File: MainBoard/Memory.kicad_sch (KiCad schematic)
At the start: 9 parts, among them U2 74AHCT04, U68 ATF22V10C, U69 CD74HC173PWR

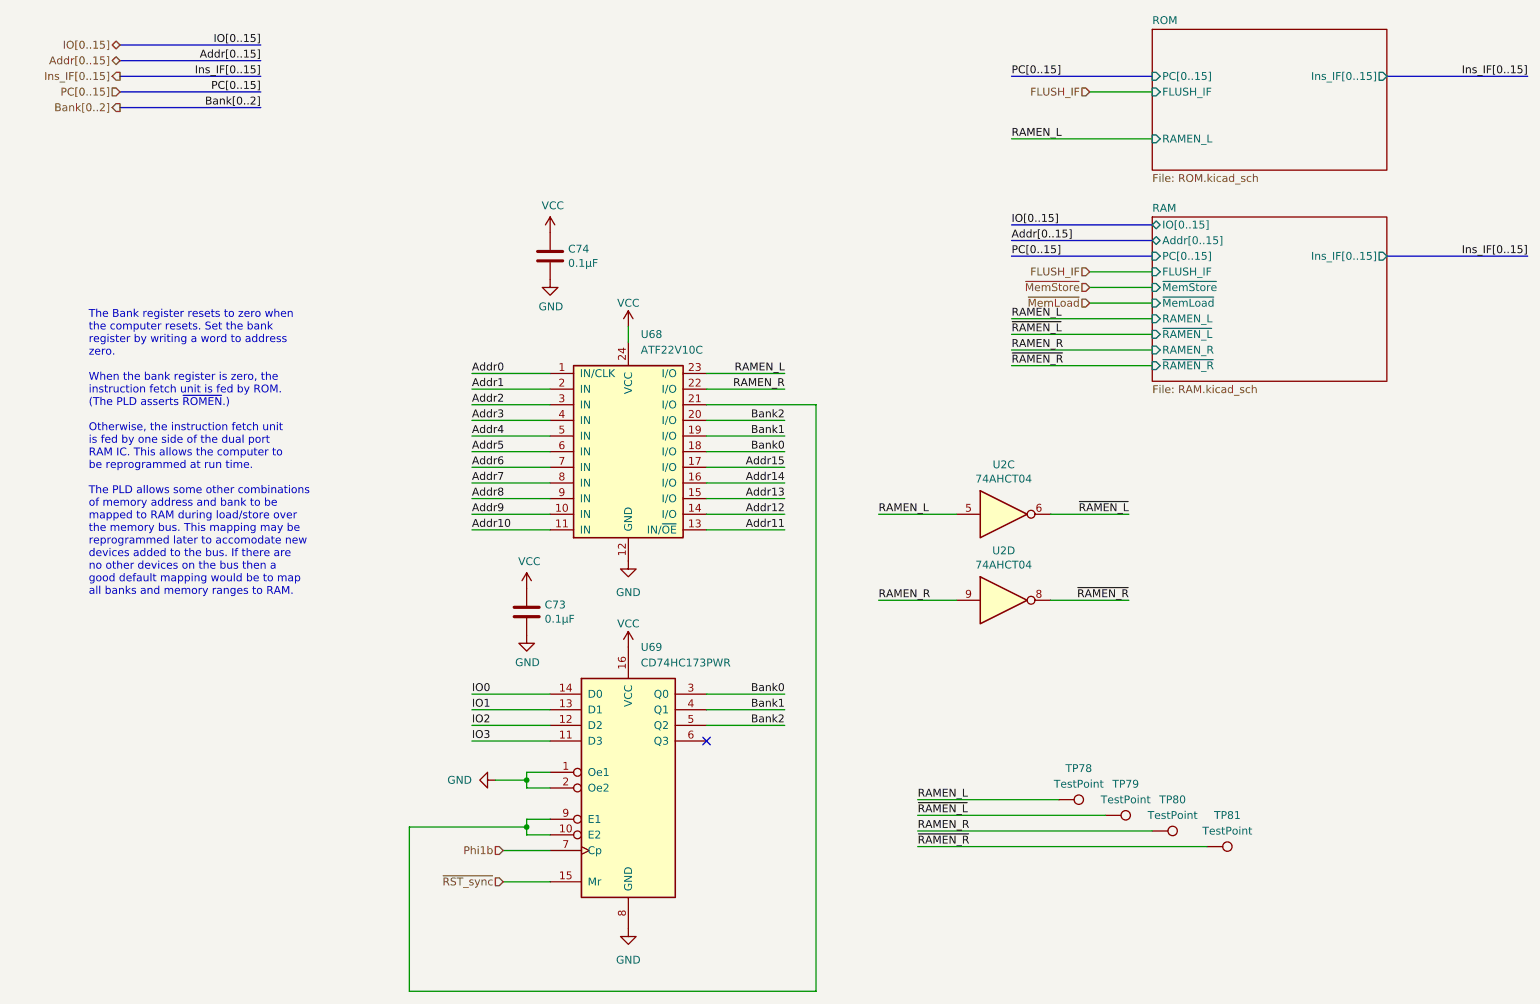
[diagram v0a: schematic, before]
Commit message: MEMModule: Fix bug in the bank register reset signal
The bank register expects an active-high reset signal but was wired to
receive an active-low signal. Fix this issue by routing /RST_sync through
an inverter first.

BUG: The MainBoard PCB layout has not been updated yet.
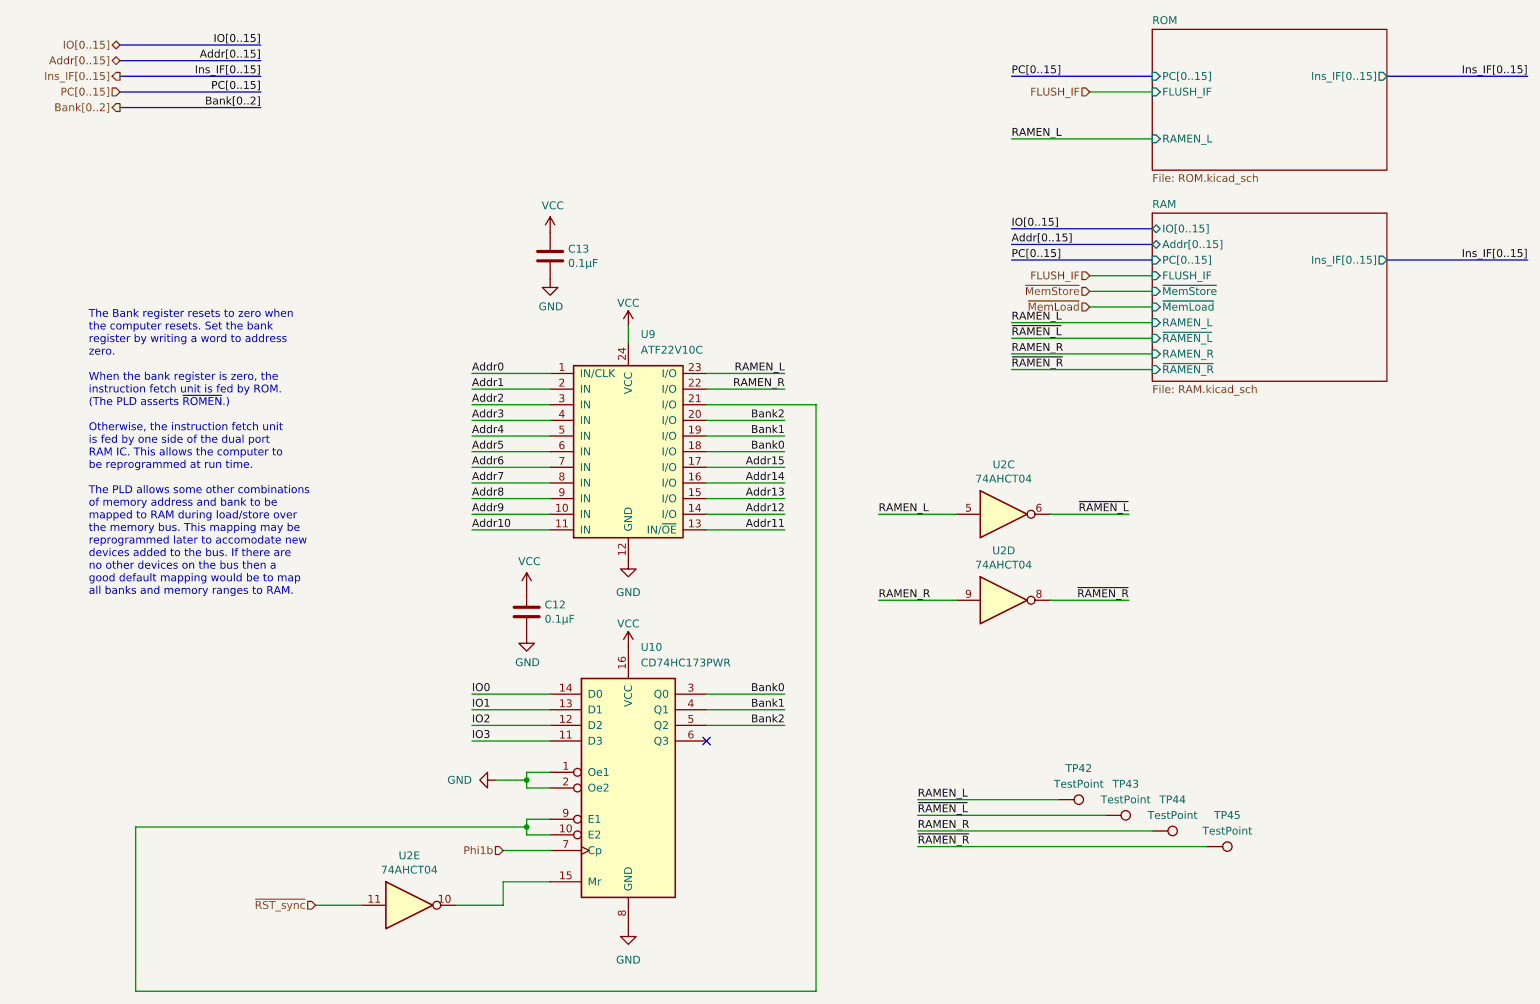
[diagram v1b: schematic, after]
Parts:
- added unit 5 of U2
- renumbered C73 to C12, C74 to C13, TP78 to TP42, TP79 to TP43, TP80 to TP44, TP81 to TP45, U69 to U10, U68 to U9
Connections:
- net ~{RST_sync}: now also U2.11; no longer U10.15 (Mr)
- new net: U10.15 (Mr), U2.10

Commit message: Update schematics for the MainBoard to include the ControleModule fix from 704c0dce
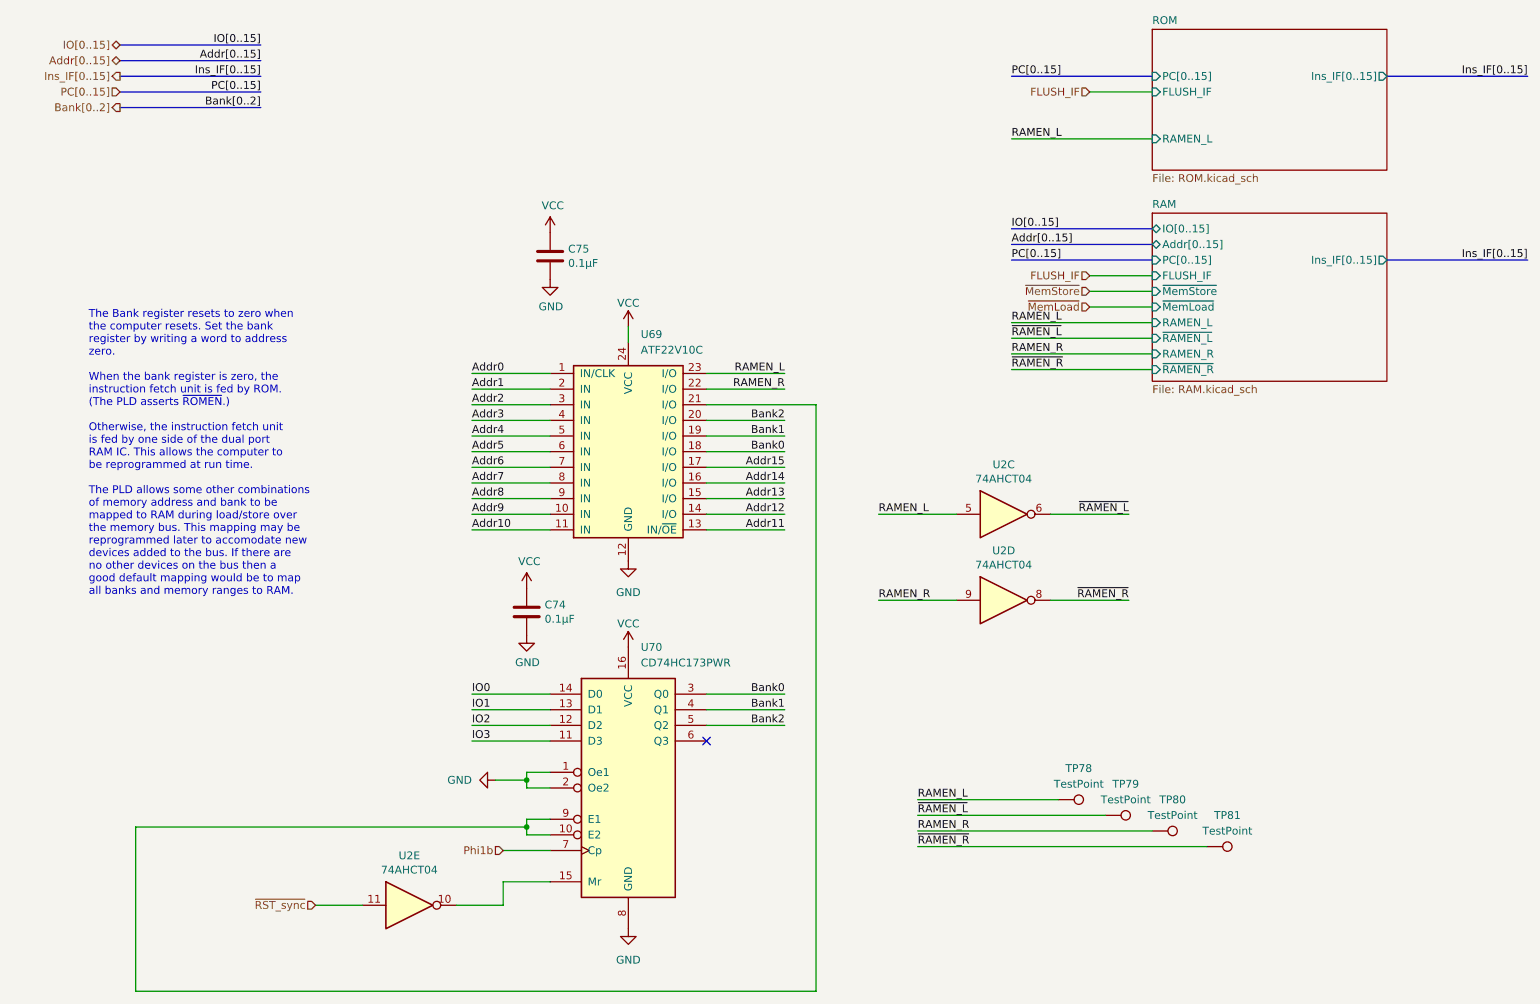
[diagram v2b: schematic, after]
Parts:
- renumbered C12 to C74, C13 to C75, TP42 to TP78, TP43 to TP79, TP44 to TP80, TP45 to TP81, U9 to U69, U10 to U70

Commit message: MainBoard: apply the MEMModule bug fix to RAM control logic
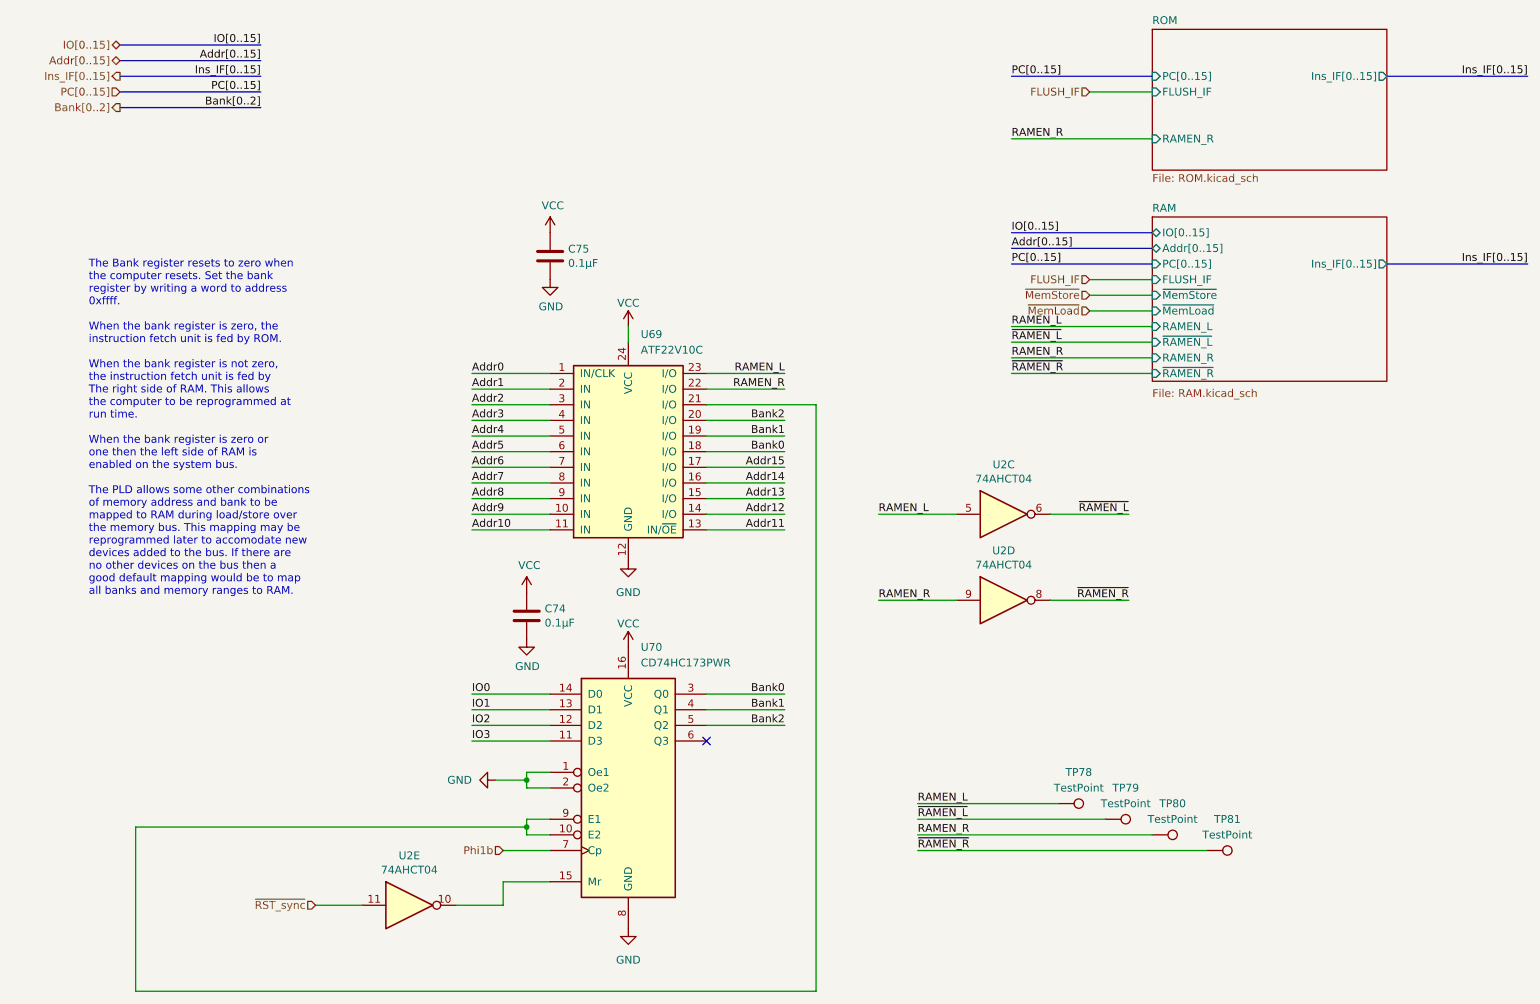
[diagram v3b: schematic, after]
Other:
- sheet ROM ports: added RAMEN_R; removed RAMEN_L
- note added: "The Bank register resets to zero when the computer resets. Set the bank register by writing a word to address 0xffff. When the bank register is zero, the instruction fetch unit is fed by ROM. When the bank register is not zero, the instruction fetch unit is fed by The right side of RAM. This allows the computer to be reprogrammed at run time. When the bank register is zero or one then the left si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"
- note removed: "The Bank register resets to zero when the computer resets. Set the bank register by writing a word to address zero. When the bank register is zero, the instruction fetch unit is fed by ROM. (The PLD asserts ~{ROMEN}.) Otherwise, the instruction fetch unit is fed by one side of the dual port RAM IC. This allows the computer to be reprogrammed at run time. The PLD allows some other combinations of 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"
- moved on the sheet: C74, TP78, TP79, TP80, TP81

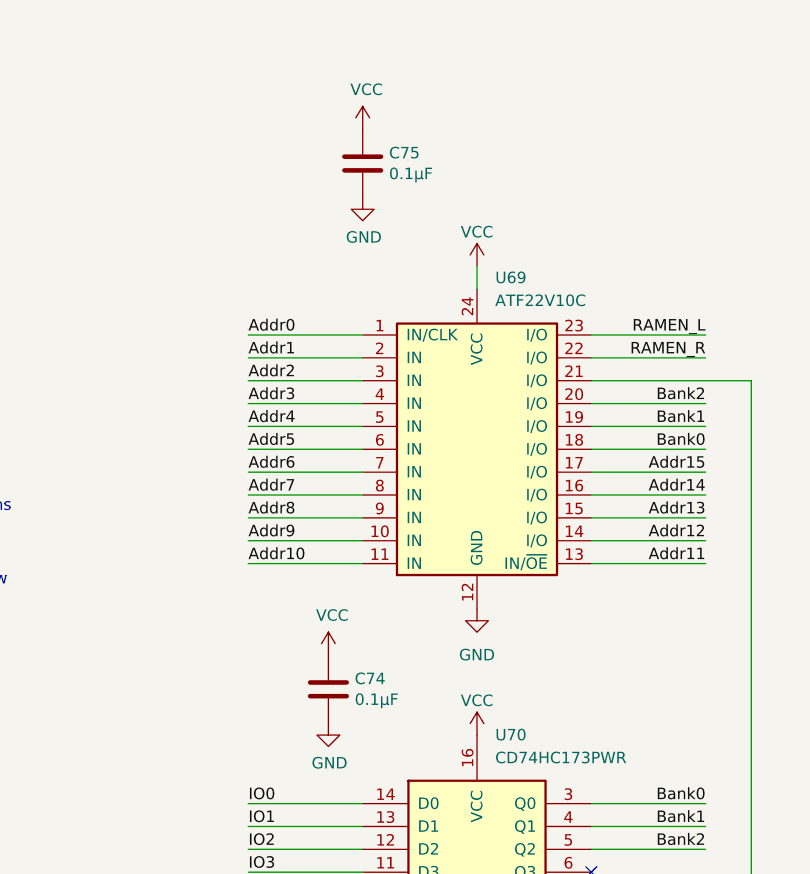
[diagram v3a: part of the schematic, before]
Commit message: MainBoard: Relabel capacitors from 100nF to 0.1uF
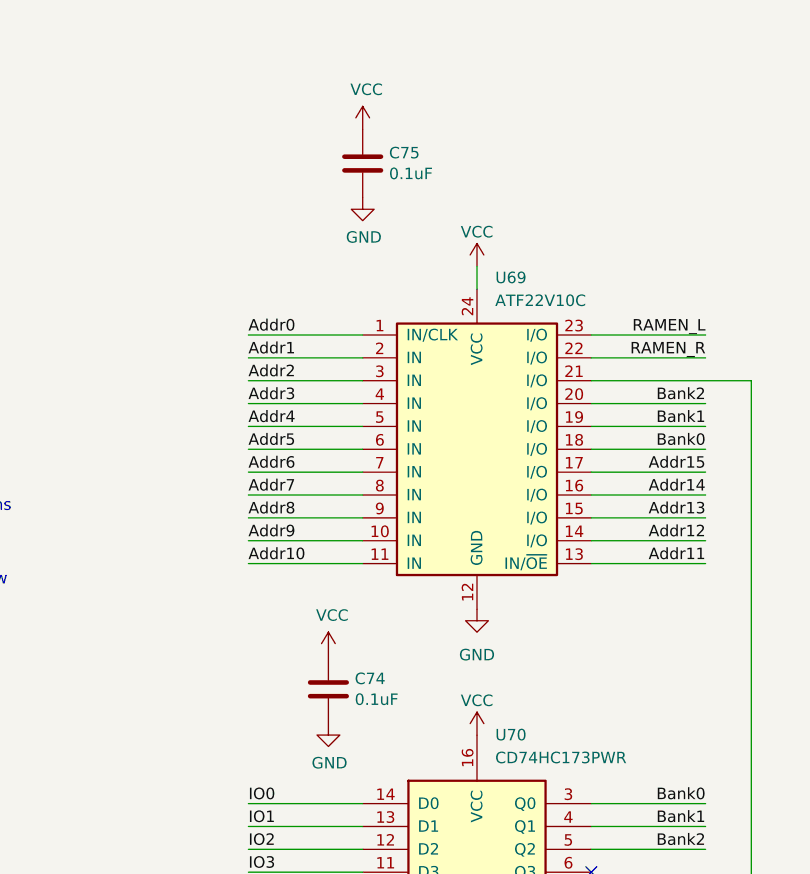
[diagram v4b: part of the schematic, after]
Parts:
- C74, C75: value 0.1μF -> 0.1uF
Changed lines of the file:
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@@
       (effects (font (size 1.27 1.27)) (justify left))
     )
-    (property "Value" "0.1μF" (at 110.871 60.833 0)
+    (property "Value" "0.1uF" (at 110.871 60.833 0)
       (effects (font (size 1.27 1.27)) (justify left))
     )
@@
       (effects (font (size 1.27 1.27)) (justify left))
     )
-    (property "Value" "0.1μF" (at 107.061 119.253 0)
+    (property "Value" "0.1uF" (at 107.061 119.253 0)
       (effects (font (size 1.27 1.27)) (justify left))
     )
